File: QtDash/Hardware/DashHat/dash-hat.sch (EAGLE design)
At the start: 91 parts, among them IC1 LM324, IC2 MCP3X083008, IC3 MCP23017SP, IC4 LM324, J1 CONN_20X2

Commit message: - finished connector 31 symbol and footprint -- still need to verify pin diameter from old dash 	- started moving components around in layout 	- added IL300 and LM158 datasheets and applicable app notes 	- fixed GND2 linking things to 3v3 for some reason -- misused GND-ISO for 12V gnd -- still need to verify that we're not crossing streams
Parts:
- added C14: 1.0uF, SparkFun-Capacitors:1.0UF-0603-16V-10%
- added D11, D12: BAT54, diode:BAT54
- added IC5, IC7: IL300, digital_dash:IL300
- added IC6: LM358D, digital_dash:LM358D
- added J6: VOLVO_CONN_31, digital_dash:VOLVO_CONN_31
- added R57, R58: 100, SparkFun-Resistors:100OHM-0603-1/10W-1%
- added R59, R60: 1M, SparkFun-Resistors:1MOHM-0603-1/4W-5%
- added R61: 10, SparkFun-Resistors:10OHM-0603-1/10W-5%
- added R62: 100k, SparkFun-Resistors:100KOHM-0603-1/10W-1%
- C11: value 10nF -> 0.1uF; device SparkFun-Capacitors:10NF-0603-50V-10% -> SparkFun-Capacitors:0.1UF-0603-25V-5%
- IC4: value LM324 -> LM358D; device digital_dash:LM324 -> digital_dash:LM358D
- R53: value 6.8k -> 1M; device SparkFun-Resistors:6.8KOHM-0603-1/10W-1% -> SparkFun-Resistors:1MOHM-0603-1/4W-5%
- R54: value 14k -> 1M; device SparkFun-Resistors:14KOHM-0603-1/10W-1% -> SparkFun-Resistors:1MOHM-0603-1/4W-5%
- R55: value 330k -> 10; device SparkFun-Resistors:330KOHM-0603-1/10W-1% -> SparkFun-Resistors:10OHM-0603-1/10W-5%
- R56: value 640k -> 100k; device SparkFun-Resistors:390KOHM-0603-1/10W-1% -> SparkFun-Resistors:100KOHM-0603-1/10W-1%
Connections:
- net N$16 renamed !SPI_CS
- removed net N$22: IC2.CH5
- new net GND-ISO: D10.A, D12.A, IC4A.V-, IC5.C1, IC7.C1, R18.1, R21.1, R24.1, R26.1, R30.1, R33.1, R36.1, R38.1, R42.1, R45.1, R48.1, R50.1, R53.1, R54.1, R59.1, R60.1
- new net N$18: IC5.C6, IC6A.-IN, R56.1
- new net N$20: IC4A.OUT, R55.1
- new net N$25: IC5.A2, R55.2
- new net N$26: IC7.A2, R61.2
- new net N$27: IC6B.-IN, IC7.C6, R62.1
- new net N$6: D11.A, D12.C, IC4B.+IN, R58.2
- new net N$8: IC4B.-IN, IC7.A4, R59.2, R60.2
- new net SIG_12V_IN2: R58.1
- new net SIG_3V3_IN2: IC2.CH5, IC6B.OUT, R62.2
- net 12V: now also C12.1, C13.1, D11.C, D9.C, IC4A.V+, IC5.C3, IC7.C3
- net 3.3V: now also C11.1, C12.2, C13.2, C14.1, IC6A.V+; no longer R18.1, R21.1, R24.1, R26.1, R30.1, R33.1, R36.1, R38.1, R42.1, R45.1, R48.1, R50.1
- net 5V: no longer C12.1, C13.1, D9.C, IC4A.V+
- net GND: now also C14.2, IC5.A5, IC6A.+IN, IC6A.V-, IC6B.+IN, IC7.A5, OK1C.EMIT, OK1D.EMIT; no longer C12.2, C13.2, D10.A, IC4A.V-, R53.1, R56.1
- net N$2: now also R57.2; no longer R53.2, R54.1
- net N$21: now also IC4B.OUT, R61.1; no longer IC2.CH4
- net N$4: now also IC5.A4, R53.2, R54.2; no longer IC4A.OUT, R55.2
- net SIG_12V_IN1: now also R57.1; no longer R54.2
- net SIG_3V3_IN1: now also IC2.CH4, IC6A.OUT; no longer C11.1, R55.1
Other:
- note added: "12V Analog Inputs (Isolated)"
- note added: "Dash Light Inputs (Isolated)"
- note added: "Resistive Sensor Inputs"
- note added: "Sensor/Analog Input ADC"
- moved on the sheet: C1, C10, C11, C12, C13, C2, C3, C4, C5, C6, C7, C8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

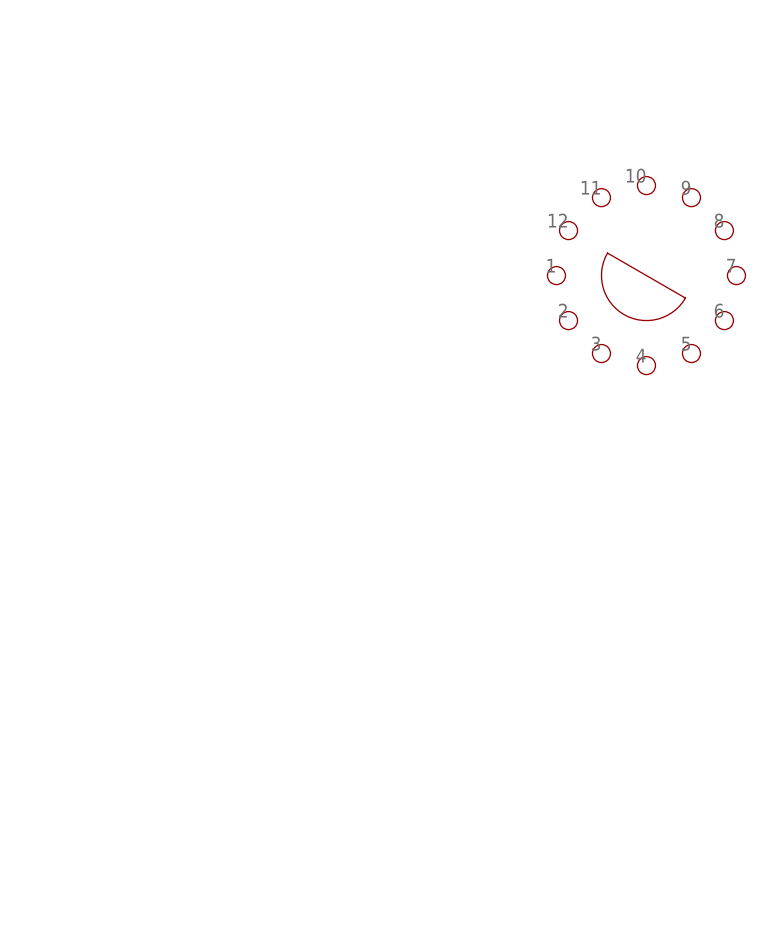
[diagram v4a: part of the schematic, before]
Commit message: - added volvo connector 32 to library and schematic -- still need to figure out where to grab 12V from
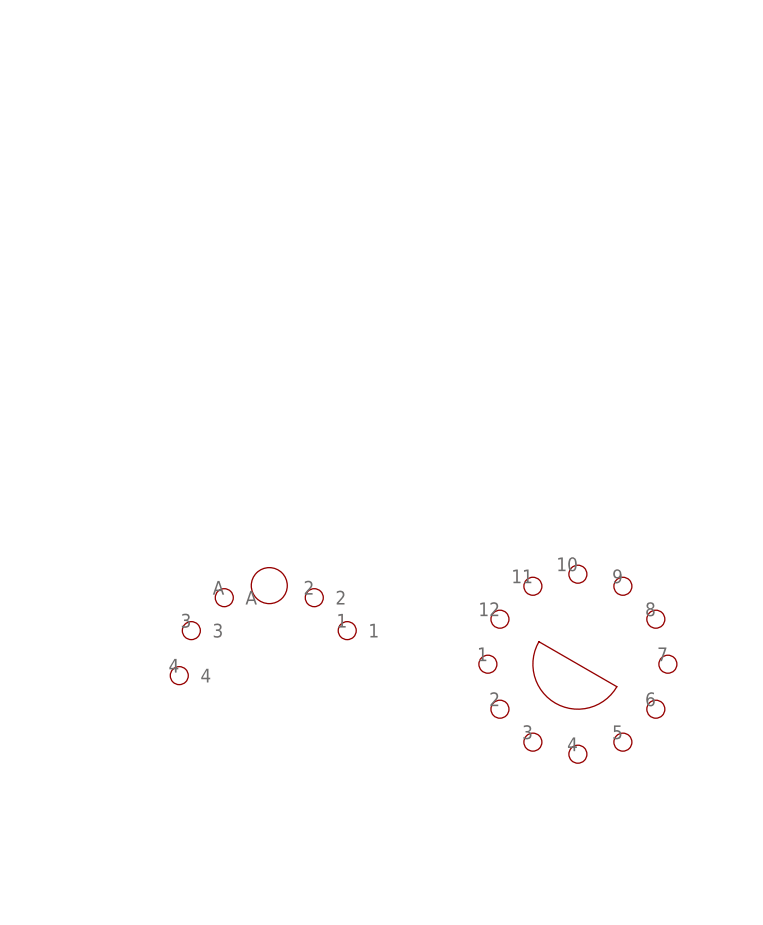
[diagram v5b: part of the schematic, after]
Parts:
- added U$1: VOLVO_CONN_32, digital_dash:VOLVO_CONN_32
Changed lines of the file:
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@@
 <setting verticaltext="up"/>
 </settings>
-<grid distance="0.05" unitdist="inch" unit="inch" style="lines" multiple="1" display="no" altdistance="0.025" altunitdist="inch" altunit="inch"/>
+<grid distance="0.1" unitdist="inch" unit="inch" style="lines" multiple="1" display="no" altdistance="0.01" altunitdist="inch" altunit="inch"/>
 <layers>
 <layer number="1" name="Top" color="4" fill="1" visible="no" active="no"/>
@@
 <part name="GND-ISO20" library="SparkFun-PowerSymbols" deviceset="GND-ISO" device=""/>
 <part name="GND-ISO21" library="SparkFun-PowerSymbols" deviceset="GND-ISO" device=""/>
+<part name="U$1" library="digital_dash" deviceset="VOLVO_CONN_32" device=""/>
 </parts>
 <sheets>
@@
 <instance part="IC4" gate="B" x="229.87" y="212.09"/>
 <instance part="IC4" gate="A" x="229.87" y="275.59"/>
-<instance part="J6" gate="G$1" x="529.59" y="260.35"/>
+<instance part="J6" gate="G$1" x="521.97" y="217.17"/>
 <instance part="GND-ISO1" gate="G$1" x="203.2" y="264.16"/>
 <instance part="GND-ISO2" gate="G$1" x="203.2" y="200.66"/>
@@
 <instance part="GND-ISO20" gate="G$1" x="259.08" y="283.21" rot="R270"/>
 <instance part="GND-ISO21" gate="G$1" x="259.08" y="219.71" rot="R270"/>
+<instance part="U$1" gate="G$1" x="487.68" y="215.9"/>
 </instances>
 <busses>

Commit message: - started layout of 12v isolated section -- will definitely have to change. 	- TODO: figure out board form factor.
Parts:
- removed U$1: VOLVO_CONN_32, digital_dash:VOLVO_CONN_32
- added J7: VOLVO_CONN_32, digital_dash:VOLVO_CONN_32
- added JP1, JP10, JP11, JP12, JP13, JP14, JP15, JP16, JP17, JP18, JP2, JP3, JP4, JP5, JP6, JP7, JP8, JP9: JUMPER-SMT_3_NO_SILK, SparkFun-Jumpers:JUMPER-SMT_3_NO_SILK
- IC3: value MCP23017SP -> MCP23017SS; device microchip:MCP23017SP -> microchip:MCP23017SS
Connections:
- new net 12V-FUSE_16: J7.A
- new net 12V-FUSE_8: J6.9
- new net AC_RELAY/VSS_TO_ECU: J6.6
- new net BLINKER_LEFT_P: J6.8, JP7.2
- new net BLINKER_RIGHT_P: J6.7, JP8.2
- new net BRAKE_FAILURE_N: J6.1, JP4.2
- new net BULB_FAILURE_N: J6.12, JP5.2
- new net CHARGING_N: J6.11, JP6.2
- new net COOLANT_TEMP_SENSOR: J6.2, JP13.3
- new net DIMMER_VOUT: J6.10, JP17.3
- new net FUEL_LVL_SENDER: J7.1, JP14.3
- new net HIGH_BEAM_P: J6.3, JP3.2
- new net IN1_12V_SIGNAL: JP17.2, R57.1
- new net N: JP9.2
- new net N$16: JP13.2, R1.1, R9.1
- new net N$19: JP10.2, JP12.2
- new net N$22: JP14.2, R10.1, R4.1
- new net N$28: JP15.3
- new net N$29: JP16.3
- new net N$30: JP15.2, R11.1, R6.1
- new net N$31: JP16.2, R12.1, R8.1
- new net N$37: J7.3
- new net OD_LAMP_P: J6.4, JP2.2
- new net OIL_PRESS_SW_N: J6.5, JP1.2
- new net PARKING_BRAKE_N: J7.2, JP11.2
- net 3.3V: no longer C12.2, C13.2
- net GND-ISO: now also C12.2, C13.2, J7.4
- net IN10N: now also JP10.3
- net IN10P: now also JP10.1
- net IN11N: now also JP11.3
- net IN11P: now also JP11.1
- net IN12N: now also JP12.3
- net IN12P: now also JP12.1
- net IN1N: now also JP1.3
- net IN1P: now also JP1.1
- net IN2N: now also JP2.3
- net IN2P: now also JP2.1
- net IN3N: now also JP3.3
- net IN3P: now also JP3.1
- net IN4N: now also JP4.3
- net IN4P: now also JP4.1
- net IN5N: now also JP5.3
- net IN5P: now also JP5.1
- net IN6N: now also JP6.3
- net IN6P: now also JP6.1
- net IN7N: now also JP7.3
- net IN7P: now also JP7.1
- net IN8N: now also JP8.3
- net IN8P: now also JP8.1
- net IN9N: now also JP9.3
- net IN9P: now also JP9.1
- net SENSOR1_IN: now also JP13.1; no longer R1.1, R9.1
- net SENSOR2_IN: now also JP14.1; no longer R10.1, R4.1
- net SENSOR3_IN: now also JP15.1; no longer R11.1, R6.1
- net SENSOR4_IN: now also JP16.1; no longer R12.1, R8.1
- net SIG_12V_IN1: now also JP17.1; no longer R57.1
- net SIG_12V_IN2: now also JP18.2
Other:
- moved on the sheet: R10, R11, R12, R9

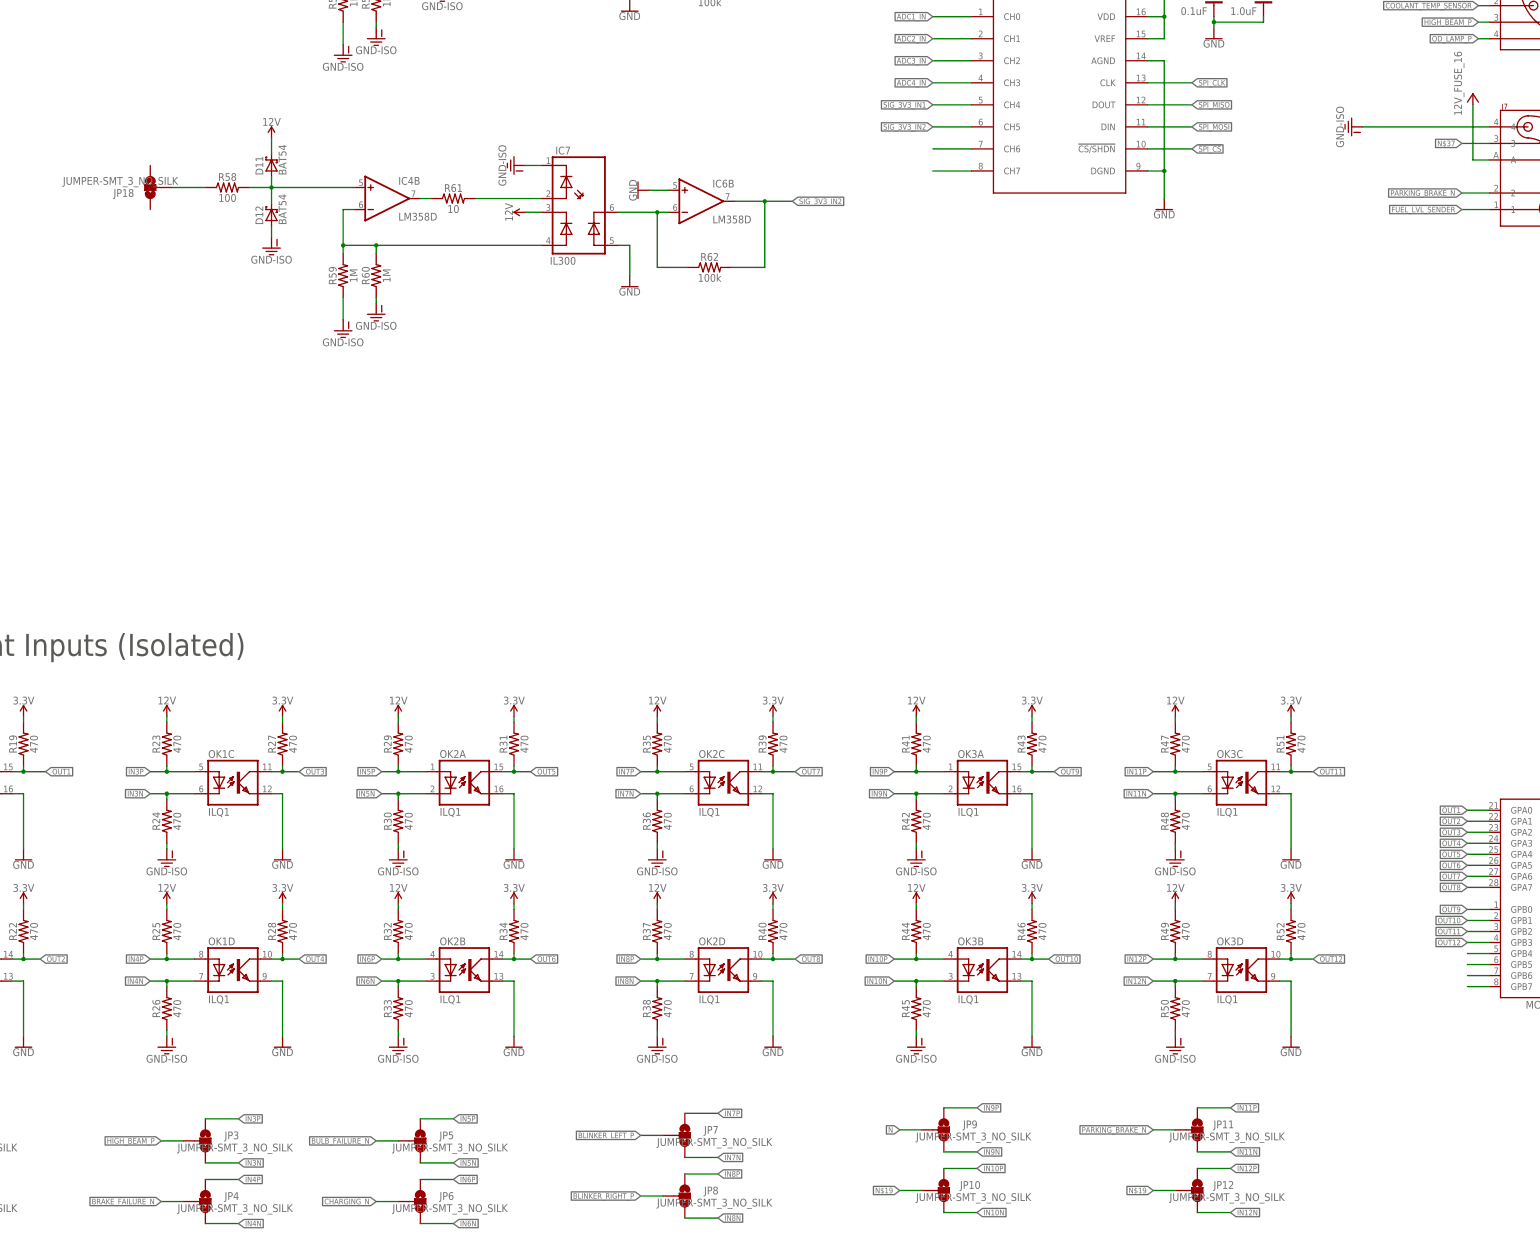
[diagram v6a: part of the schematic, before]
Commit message: - added MCP23017 user space driver in QtDash project using linux i2c-dev -- tested using mcp23017 i2c breakout board hooked up to i2c1 on pi 	- Hooked up indicator lights and blinkers in qt program 	- re-arranged board layout -- moved around 12V signals and hooked up 12V fuse 6 to second 12V analog input 	- changed i2c-bcm2835 to be built into the kernel instead of loaded as a module 	- TODO: add MAP sensor input to one of the analog inputs 	- TODO: clean up and document dash lights -- attempt to make configurable as this is the area that will differ most between 240 years 	- TODO: add interface for MCP3208 -- will have to try sysfs approach before making a user space driver 	- TODO: start figuring out packaging for screen/pcb/pi/power supplies in the 240 dash
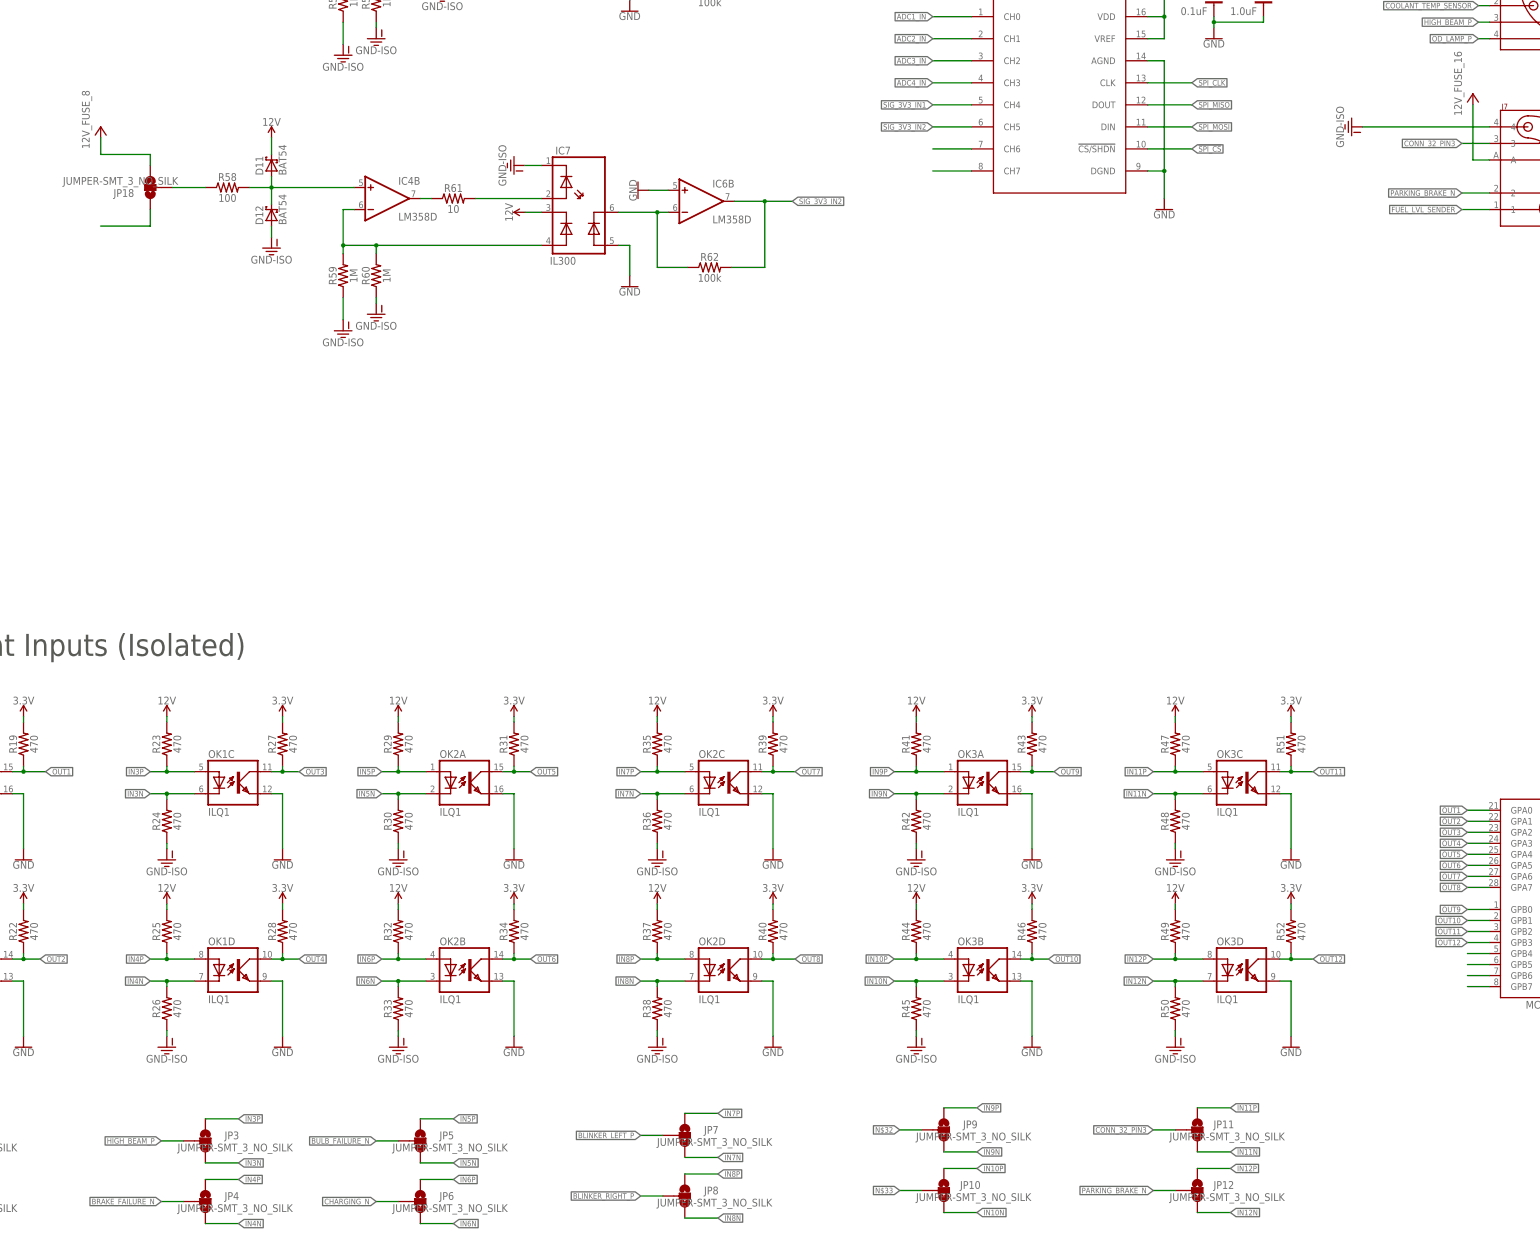
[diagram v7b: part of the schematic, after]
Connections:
- net N renamed N$32
- removed net N$19: JP10.2, JP12.2
- removed net N$37: J7.3
- new net CONN_32_PIN3: J7.3, JP11.2
- new net N$33: JP10.2
- new net N$34: JP18.1
- net 12V-FUSE_8: now also JP18.3
- net PARKING_BRAKE_N: now also JP12.2; no longer JP11.2
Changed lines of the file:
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@@
 <setting verticaltext="up"/>
 </settings>
-<grid distance="0.1" unitdist="inch" unit="inch" style="lines" multiple="1" display="no" altdistance="0.01" altunitdist="inch" altunit="inch"/>
+<grid distance="0.05" unitdist="inch" unit="inch" style="lines" multiple="1" display="no" altdistance="0.01" altunitdist="inch" altunit="inch"/>
 <layers>
 <layer number="1" name="Top" color="4" fill="1" visible="no" active="no"/>
@@
 <part name="U$2" library="digital_dash" deviceset="12V_FUSE_16" device=""/>
 <part name="GND-ISO23" library="SparkFun-PowerSymbols" deviceset="GND-ISO" device=""/>
+<part name="U$3" library="digital_dash" deviceset="12V_FUSE_8" device=""/>
 </parts>
 <sheets>
@@
 <instance part="U$2" gate="G$1" x="480.06" y="233.68"/>
 <instance part="GND-ISO23" gate="G$1" x="214.63" y="283.21"/>
+<instance part="U$3" gate="G$1" x="163.83" y="226.06"/>
 </instances>
 <busses>
@@
 </segment>
 </net>
-<net name="N$37" class="0">
+<net name="CONN_32_PIN3" class="0">
 <segment>
 <pinref part="J7" gate="G$1" pin="3"/>
@@
 <label x="477.52" y="224.79" size="1.27" layer="95" rot="R180" xref="yes"/>
 </segment>
+<segment>
+<pinref part="JP11" gate="G$1" pin="2"/>
+<wire x1="411.48" y1="-2.54" x2="406.4" y2="-2.54" width="0.1524" layer="91"/>
+<label x="406.4" y="-2.54" size="1.27" layer="95" rot="R180" xref="yes"/>
+</segment>
 </net>
 <net name="PARKING_BRAKE_N" class="0">
@@
 </segment>
 <segment>
-<pinref part="JP11" gate="G$1" pin="2"/>
-<wire x1="411.48" y1="-2.54" x2="406.4" y2="-2.54" width="0.1524" layer="91"/>
-<label x="406.4" y="-2.54" size="1.27" layer="95" rot="R180" xref="yes"/>
+<pinref part="JP12" gate="G$1" pin="2"/>
+<wire x1="411.48" y1="-16.51" x2="406.4" y2="-16.51" width="0.1524" layer="91"/>
+<label x="406.4" y="-16.51" size="1.27" layer="95" rot="R180" xref="yes"/>
 </segment>
 </net>
@@
 <label x="17.78" y="228.6" size="1.27" layer="95" rot="R180" xref="yes"/>
 <pinref part="JP14" gate="G$1" pin="3"/>
-</segment>
-</net>
-<net name="N$19" class="0">
-<segment>
-<pinref part="JP10" gate="G$1" pin="2"/>
-<wire x1="353.06" y1="-16.51" x2="347.98" y2="-16.51" width="0.1524" layer="91"/>
-<label x="347.98" y="-16.51" size="1.27" layer="95" rot="R180" xref="yes"/>
-</segment>
-<segment>
-<pinref part="JP12" gate="G$1" pin="2"/>
-<wire x1="411.48" y1="-16.51" x2="406.4" y2="-16.51" width="0.1524" layer="91"/>
-<label x="406.4" y="-16.51" size="1.27" layer="95" rot="R180" xref="yes"/>
-</segment>
-</net>
-<net name="N" class="0">
-<segment>
-<pinref part="JP9" gate="G$1" pin="2"/>
-<wire x1="353.06" y1="-2.54" x2="347.98" y2="-2.54" width="0.1524" layer="91"/>
-<label x="347.98" y="-2.54" size="1.27" layer="95" rot="R180" xref="yes"/>
 </segment>
 </net>
@@
 <pinref part="U$1" gate="G$1" pin="12V-FUSE_8"/>
 </segment>
+<segment>
+<pinref part="JP18" gate="G$1" pin="3"/>
+<wire x1="175.26" y1="219.71" x2="175.26" y2="222.25" width="0.1524" layer="91"/>
+<wire x1="175.26" y1="222.25" x2="163.83" y2="222.25" width="0.1524" layer="91"/>
+<pinref part="U$3" gate="G$1" pin="12V-FUSE_8"/>
+<wire x1="163.83" y1="222.25" x2="163.83" y2="226.06" width="0.1524" layer="91"/>
+</segment>
 </net>
 <net name="12V-FUSE_16" class="0">
@@
 </segment>
 </net>
+<net name="N$32" class="0">
+<segment>
+<pinref part="JP9" gate="G$1" pin="2"/>
+<wire x1="353.06" y1="-2.54" x2="347.98" y2="-2.54" width="0.1524" layer="91"/>
+<label x="347.98" y="-2.54" size="1.27" layer="95" rot="R180" xref="yes"/>
+</segment>
+</net>
+<net name="N$33" class="0">
+<segment>
+<pinref part="JP10" gate="G$1" pin="2"/>
+<wire x1="353.06" y1="-16.51" x2="347.98" y2="-16.51" width="0.1524" layer="91"/>
+<label x="347.98" y="-16.51" size="1.27" layer="95" rot="R180" xref="yes"/>
+</segment>
+</net>
+<net name="N$34" class="0">
+<segment>
+<pinref part="JP18" gate="G$1" pin="1"/>
+<wire x1="175.26" y1="209.55" x2="175.26" y2="205.74" width="0.1524" layer="91"/>
+<wire x1="175.26" y1="205.74" x2="163.83" y2="205.74" width="0.1524" layer="91"/>
+</segment>
+</net>
